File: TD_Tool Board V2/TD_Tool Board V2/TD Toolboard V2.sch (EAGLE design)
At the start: 142 parts, among them J3 430450400CON_430450400_MOL, M1 NMOSFET_WSD3066DN33, M2 CJ3400, M3 CJ3400, M4 CJ3400, P1 TPS54202_BUCKCONV, P2 3.3V, U1 RP2040IC57_RP2040-L, U2 W25Q128JVSIQSOIC_128JVSIQ_WIN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, U3 SN65HVD1050DRD8-L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

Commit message: TMC routed
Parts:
- removed IO3: TEST-POINT3, SparkFun-Connectors:TEST-POINT3
- removed X4: JST-XH-04-PIN-LONG-PAD, Rembrandt Electronics - JST XH Connectors v1-0:JST-XH-04-PIN-LONG-PAD
- added EXTRUDER: JST-XH-04-PIN-LONG-PAD, Rembrandt Electronics - JST XH Connectors v1-0:JST-XH-04-PIN-LONG-PAD
- L2: value ACM2012-201-2P-T002ACM2012_TDK -> ACM2012
- U3: value SN65HVD1050DRD8-L -> SN65HVD
- U7: value TMC2209-LA-TQFN28_5X5_3X8_EPAD_TRI -> TMC2209
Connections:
- net +5V: no longer IO3.1
- net A1: now also EXTRUDER-2.S; no longer X4-2.S
- net A2: now also EXTRUDER-1.S; no longer X4-1.S
- net B1: now also EXTRUDER-3.S; no longer X4-3.S
- net B2: now also EXTRUDER-4.S; no longer X4-4.S
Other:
- moved on the sheet: A1, A2, B1, B2
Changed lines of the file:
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@@
 <part name="SUPPLY48" library="Power_Symbols" deviceset="+3.3V" device="" value="+3.3V"/>
 <part name="SUPPLY49" library="Power_Symbols" deviceset="+3.3V" device="" value="+3.3V"/>
-<part name="U3" library="Fracktal Misc Lib" library_urn="urn:adsk.wipprod:fs.file:vf.Pfq9Q3azRLuASzDebw0K2A" deviceset="SN65HVD1050DR" device="D8-L">
+<part name="U3" library="Fracktal Misc Lib" library_urn="urn:adsk.wipprod:fs.file:vf.Pfq9Q3azRLuASzDebw0K2A" deviceset="SN65HVD1050DR" device="D8-L" value="SN65HVD">
 <attribute name="LCSCPN#" value="C14019"/>
 </part>
@@
 <attribute name="LCSCPN#" value="C25079"/>
 </part>
-<part name="L2" library="2023-04-02_14-21-16_Library" deviceset="ACM2012-201-2P-T002" device="ACM2012_TDK">
+<part name="L2" library="2023-04-02_14-21-16_Library" deviceset="ACM2012-201-2P-T002" device="ACM2012_TDK" value="ACM2012">
 <attribute name="LCSCPN#" value="C3029258"/>
 </part>
 <part name="SJ1" library="SparkFun-Retired" deviceset="SOLDERJUMPER" device="TRACE"/>
-<part name="U7" library="Fracktal Misc Lib" library_urn="urn:adsk.wipprod:fs.file:vf.Pfq9Q3azRLuASzDebw0K2A" deviceset="TMC2209-LA-T" device="QFN28_5X5_3X8_EPAD_TRI" value="TMC2209-LA-TQFN28_5X5_3X8_EPAD_TRI">
+<part name="U7" library="Fracktal Misc Lib" library_urn="urn:adsk.wipprod:fs.file:vf.Pfq9Q3azRLuASzDebw0K2A" deviceset="TMC2209-LA-T" device="QFN28_5X5_3X8_EPAD_TRI" value="TMC2209">
 <attribute name="LCSCPN#" value="C2150710"/>
 </part>
@@
 <part name="IO1" library="SparkFun-Connectors" library_urn="urn:adsk.eagle:library:513" deviceset="TEST-POINT" device="3" package3d_urn="urn:adsk.eagle:package:38286/1"/>
 <part name="IO2" library="SparkFun-Connectors" library_urn="urn:adsk.eagle:library:513" deviceset="TEST-POINT" device="3" package3d_urn="urn:adsk.eagle:package:38286/1"/>
-<part name="IO3" library="SparkFun-Connectors" library_urn="urn:adsk.eagle:library:513" deviceset="TEST-POINT" device="3" package3d_urn="urn:adsk.eagle:package:38286/1"/>
 <part name="SJ3" library="SparkFun-Retired" deviceset="SOLDERJUMPER" device="TRACE"/>
 <part name="SUPPLY68" library="Power_Symbols" deviceset="+12V" device="" value="+24V"/>
@@
 <part name="B1" library="SparkFun-Connectors" library_urn="urn:adsk.eagle:library:513" deviceset="TEST-POINT" device="3X4" package3d_urn="urn:adsk.eagle:package:38287/1"/>
 <part name="B2" library="SparkFun-Connectors" library_urn="urn:adsk.eagle:library:513" deviceset="TEST-POINT" device="3X4" package3d_urn="urn:adsk.eagle:package:38287/1"/>
-<part name="X4" library="Rembrandt Electronics - JST XH Connectors v1-0" deviceset="JST-XH-04-PIN" device="-LONG-PAD">
+<part name="EXTRUDER" library="Rembrandt Electronics - JST XH Connectors v1-0" deviceset="JST-XH-04-PIN" device="-LONG-PAD">
 <attribute name="EXTRUDER" value=""/>
 </part>
@@
 <attribute name="NAME" x="356.87" y="-131.064" size="1.27" layer="95" font="vector" rot="R180" align="center-left"/>
 </instance>
-<instance part="IO3" gate="G$1" x="370.84" y="-120.904" smashed="yes" rot="R180">
-<attribute name="NAME" x="367.03" y="-120.904" size="1.27" layer="95" font="vector" rot="R180" align="center-left"/>
-</instance>
 <instance part="SJ3" gate="1" x="439.42" y="-104.14" smashed="yes">
 <attribute name="NAME" x="436.88" y="-101.6" size="1.778" layer="95"/>
@@
 <attribute name="NAME" x="429.26" y="-208.28" size="1.778" layer="95" font="vector"/>
 </instance>
-<instance part="A2" gate="G$1" x="368.3" y="-264.16" smashed="yes">
-<attribute name="NAME" x="373.38" y="-264.16" size="1.778" layer="95" font="vector"/>
-</instance>
-<instance part="A1" gate="G$1" x="368.3" y="-261.62" smashed="yes">
-<attribute name="NAME" x="373.38" y="-261.62" size="1.778" layer="95" font="vector"/>
-</instance>
-<instance part="B1" gate="G$1" x="368.3" y="-259.08" smashed="yes">
-<attribute name="NAME" x="373.38" y="-259.08" size="1.778" layer="95" font="vector"/>
-</instance>
-<instance part="B2" gate="G$1" x="368.3" y="-256.54" smashed="yes">
-<attribute name="NAME" x="373.38" y="-256.54" size="1.778" layer="95" font="vector"/>
-</instance>
-<instance part="X4" gate="-1" x="340.36" y="-264.16" smashed="yes" rot="R180">
-<attribute name="NAME" x="337.82" y="-263.398" size="1.524" layer="95" rot="R180"/>
-<attribute name="VALUE" x="341.122" y="-265.557" size="1.778" layer="96" rot="R180"/>
-<attribute name="EXTRUDER" x="342.9" y="-254" size="1.778" layer="96" rot="R180" display="name"/>
-</instance>
-<instance part="X4" gate="-2" x="340.36" y="-261.62" smashed="yes" rot="R180">
-<attribute name="NAME" x="337.82" y="-260.858" size="1.524" layer="95" rot="R180"/>
-</instance>
-<instance part="X4" gate="-3" x="340.36" y="-259.08" smashed="yes" rot="R180">
-<attribute name="NAME" x="337.82" y="-258.318" size="1.524" layer="95" rot="R180"/>
-</instance>
-<instance part="X4" gate="-4" x="340.36" y="-256.54" smashed="yes" rot="R180">
-<attribute name="NAME" x="337.82" y="-255.778" size="1.524" layer="95" rot="R180"/>
+<instance part="A2" gate="G$1" x="393.7" y="-264.16" smashed="yes">
+<attribute name="NAME" x="398.78" y="-264.16" size="1.778" layer="95" font="vector"/>
+</instance>
+<instance part="A1" gate="G$1" x="393.7" y="-261.62" smashed="yes">
+<attribute name="NAME" x="398.78" y="-261.62" size="1.778" layer="95" font="vector"/>
+</instance>
+<instance part="B1" gate="G$1" x="393.7" y="-259.08" smashed="yes">
+<attribute name="NAME" x="398.78" y="-259.08" size="1.778" layer="95" font="vector"/>
+</instance>
+<instance part="B2" gate="G$1" x="393.7" y="-256.54" smashed="yes">
+<attribute name="NAME" x="398.78" y="-256.54" size="1.778" layer="95" font="vector"/>
+</instance>
+<instance part="EXTRUDER" gate="-1" x="365.76" y="-264.16" smashed="yes" rot="R180">
+<attribute name="NAME" x="363.22" y="-263.398" size="1.524" layer="95" rot="R180"/>
+<attribute name="VALUE" x="366.522" y="-265.557" size="1.778" layer="96" rot="R180"/>
+<attribute name="EXTRUDER" x="368.3" y="-254" size="1.778" layer="96" rot="R180" display="name"/>
+</instance>
+<instance part="EXTRUDER" gate="-2" x="365.76" y="-261.62" smashed="yes" rot="R180">
+<attribute name="NAME" x="363.22" y="-260.858" size="1.524" layer="95" rot="R180"/>
+</instance>
+<instance part="EXTRUDER" gate="-3" x="365.76" y="-259.08" smashed="yes" rot="R180">
+<attribute name="NAME" x="363.22" y="-258.318" size="1.524" layer="95" rot="R180"/>
+</instance>
+<instance part="EXTRUDER" gate="-4" x="365.76" y="-256.54" smashed="yes" rot="R180">
+<attribute name="NAME" x="363.22" y="-255.778" size="1.524" layer="95" rot="R180"/>
 </instance>
 <instance part="M2" gate="G$1" x="373.38" y="-370.84" smashed="yes">
@@
 <wire x1="403.86" y1="-127" x2="383.54" y2="-127" width="0.1524" layer="91"/>
 <pinref part="SUPPLY34" gate="G$1" pin="+5V"/>
-<wire x1="383.54" y1="-127" x2="383.54" y2="-119.38" width="0.1524" layer="91"/>
-<junction x="383.54" y="-127"/>
-<pinref part="IO3" gate="G$1" pin="1"/>
-<wire x1="383.54" y1="-119.38" x2="370.84" y2="-119.38" width="0.1524" layer="91"/>
-<wire x1="370.84" y1="-119.38" x2="370.84" y2="-120.904" width="0.1524" layer="91"/>
 </segment>
 </net>
@@
 </segment>
 <segment>
-<label x="358.14" y="-256.54" size="1.27" layer="95" xref="yes"/>
+<label x="383.54" y="-256.54" size="1.27" layer="95" xref="yes"/>
 <pinref part="B2" gate="G$1" pin="1"/>
-<wire x1="368.3" y1="-256.54" x2="342.9" y2="-256.54" width="0.1524" layer="91"/>
-<pinref part="X4" gate="-4" pin="S"/>
+<wire x1="393.7" y1="-256.54" x2="368.3" y2="-256.54" width="0.1524" layer="91"/>
+<pinref part="EXTRUDER" gate="-4" pin="S"/>
 </segment>
 </net>
@@
 </segment>
 <segment>
-<wire x1="342.9" y1="-264.16" x2="368.3" y2="-264.16" width="0.1524" layer="91"/>
-<label x="358.14" y="-264.16" size="1.27" layer="95" xref="yes"/>
+<wire x1="368.3" y1="-264.16" x2="393.7" y2="-264.16" width="0.1524" layer="91"/>
+<label x="383.54" y="-264.16" size="1.27" layer="95" xref="yes"/>
 <pinref part="A2" gate="G$1" pin="1"/>
-<pinref part="X4" gate="-1" pin="S"/>
+<pinref part="EXTRUDER" gate="-1" pin="S"/>
 </segment>
 </net>
@@
 </segment>
 <segment>
-<wire x1="342.9" y1="-261.62" x2="368.3" y2="-261.62" width="0.1524" layer="91"/>
-<label x="358.14" y="-261.62" size="1.27" layer="95" xref="yes"/>
+<wire x1="368.3" y1="-261.62" x2="393.7" y2="-261.62" width="0.1524" layer="91"/>
+<label x="383.54" y="-261.62" size="1.27" layer="95" xref="yes"/>
 <pinref part="A1" gate="G$1" pin="1"/>
-<pinref part="X4" gate="-2" pin="S"/>
+<pinref part="EXTRUDER" gate="-2" pin="S"/>
 </segment>
 </net>
@@
 </segment>
 <segment>
-<wire x1="342.9" y1="-259.08" x2="368.3" y2="-259.08" width="0.1524" layer="91"/>
-<label x="358.14" y="-259.08" size="1.27" layer="95" xref="yes"/>
+<wire x1="368.3" y1="-259.08" x2="393.7" y2="-259.08" width="0.1524" layer="91"/>
+<label x="383.54" y="-259.08" size="1.27" layer="95" xref="yes"/>
 <pinref part="B1" gate="G$1" pin="1"/>
-<pinref part="X4" gate="-3" pin="S"/>
-</segment>
-</net>
+<pinref part="EXTRUDER" gate="-3" pin="S"/>
+</segment>
+</net>

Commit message: Placed other connectors and re arranged adxl345
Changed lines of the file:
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@@
 </segment>
 <segment>
-<wire x1="378.46" y1="-363.29" x2="386.08" y2="-363.29" width="0.1524" layer="91"/>
 <wire x1="386.08" y1="-363.29" x2="386.08" y2="-363.22" width="0.1524" layer="91"/>
 <pinref part="SUPPLY87" gate="G$1" pin="+12V"/>
@@
 <pinref part="C42" gate="G$1" pin="1"/>
 <junction x="386.08" y="-363.22"/>
-<wire x1="378.46" y1="-363.29" x2="378.46" y2="-342.9" width="0.1524" layer="91"/>
+<wire x1="386.08" y1="-363.22" x2="378.46" y2="-363.22" width="0.1524" layer="91"/>
 <pinref part="X5" gate="-2" pin="S"/>
+<wire x1="378.46" y1="-363.22" x2="378.46" y2="-342.9" width="0.1524" layer="91"/>
 </segment>
 <segment>
@@
 <segment>
 <pinref part="M2" gate="G$1" pin="D"/>
+<pinref part="X5" gate="-1" pin="S"/>
 <wire x1="375.92" y1="-365.76" x2="375.92" y2="-342.9" width="0.1524" layer="91"/>
-<pinref part="X5" gate="-1" pin="S"/>
-</segment>
-</net>
+</segment>
+</net>

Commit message: Finished routing all components
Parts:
- removed FD1, FD2, FD3: FIDUCIAL, CDC Library:FIDUCIAL
- D9: device LED:CHIP-FLAT-G_0603-0.35MM -> led:LED3MM
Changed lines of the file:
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@@
 <layers>
 <layer number="1" name="Top" color="4" fill="1" visible="no" active="no"/>
+<layer number="2" name="Route2" color="1" fill="3" visible="no" active="no"/>
+<layer number="3" name="Route3" color="4" fill="3" visible="no" active="no"/>
+<layer number="4" name="Route4" color="1" fill="4" visible="no" active="no"/>
+<layer number="5" name="Route5" color="4" fill="4" visible="no" active="no"/>
+<layer number="6" name="Route6" color="1" fill="8" visible="no" active="no"/>
+<layer number="7" name="Route7" color="4" fill="8" visible="no" active="no"/>
+<layer number="8" name="Route8" color="1" fill="2" visible="no" active="no"/>
+<layer number="9" name="Route9" color="4" fill="2" visible="no" active="no"/>
+<layer number="10" name="Route10" color="1" fill="7" visible="no" active="no"/>
+<layer number="11" name="Route11" color="4" fill="7" visible="no" active="no"/>
+<layer number="12" name="Route12" color="1" fill="5" visible="no" active="no"/>
+<layer number="13" name="Route13" color="4" fill="5" visible="no" active="no"/>
+<layer number="14" name="Route14" color="1" fill="6" visible="no" active="no"/>
+<layer number="15" name="Route15" color="4" fill="6" visible="no" active="no"/>
 <layer number="16" name="Bottom" color="1" fill="1" visible="no" active="no"/>
 <layer number="17" name="Pads" color="2" fill="1" visible="no" active="no"/>
@@
 <attribute name="LCSCPN#" value="C25087"/>
 </part>
-<part name="FD1" library="CDC Library" library_urn="urn:adsk.wipprod:fs.file:vf.SXBn864FQp6MR9sO0qnWLQ" deviceset="FIDUCIAL" device="" package3d_urn="urn:adsk.eagle:package:6240632/1"/>
-<part name="FD2" library="CDC Library" library_urn="urn:adsk.wipprod:fs.file:vf.SXBn864FQp6MR9sO0qnWLQ" deviceset="FIDUCIAL" device="" package3d_urn="urn:adsk.eagle:package:6240632/1"/>
-<part name="FD3" library="CDC Library" library_urn="urn:adsk.wipprod:fs.file:vf.SXBn864FQp6MR9sO0qnWLQ" deviceset="FIDUCIAL" device="" package3d_urn="urn:adsk.eagle:package:6240632/1"/>
 <part name="FD4" library="CDC Library" library_urn="urn:adsk.wipprod:fs.file:vf.SXBn864FQp6MR9sO0qnWLQ" deviceset="FIDUCIAL" device="" package3d_urn="urn:adsk.eagle:package:6240632/1"/>
 <part name="FD5" library="CDC Library" library_urn="urn:adsk.wipprod:fs.file:vf.SXBn864FQp6MR9sO0qnWLQ" deviceset="FIDUCIAL" device="" package3d_urn="urn:adsk.eagle:package:6240632/1"/>
@@
 <attribute name="LCSCPN#" value="C25086"/>
 </part>
-<part name="D9" library="LED" deviceset="CHIP-FLAT-G" device="_0603-0.35MM" package3d_urn="urn:adsk.eagle:package:24294786/1" value="LED_G">
+<part name="D9" library="led" library_urn="urn:adsk.eagle:library:259" deviceset="LED" device="3MM" package3d_urn="urn:adsk.eagle:package:15797/1" value="LED_G">
 <attribute name="LCSCPN#" value="C72043"/>
 </part>
@@
 <attribute name="LCSCPN#" x="307.34" y="-17.78" size="1.27" layer="96" rot="R90" align="center-right" display="off"/>
 </instance>
-<instance part="FD1" gate="G$1" x="167.64" y="7.62" smashed="yes"/>
-<instance part="FD2" gate="G$1" x="172.72" y="7.62" smashed="yes"/>
-<instance part="FD3" gate="G$1" x="177.8" y="7.62" smashed="yes"/>
 <instance part="FD4" gate="G$1" x="167.64" y="2.54" smashed="yes"/>
 <instance part="FD5" gate="G$1" x="172.72" y="2.54" smashed="yes"/>
@@
 <instance part="D9" gate="G$1" x="193.04" y="-50.8" smashed="yes" rot="R270">
 <attribute name="NAME" x="187.198" y="-50.546" size="1.778" layer="95" rot="R180" align="top-right"/>
-<attribute name="VALUE" x="186.436" y="-54.356" size="1.778" layer="96" rot="R180" align="top-right"/>
 <attribute name="LCSCPN#" x="193.04" y="-50.8" size="1.778" layer="96" rot="R270" display="off"/>
 </instance>

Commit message: Fixed font sizes, added lables
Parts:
- C_FAN2: value JST-XH-02-PIN-LONG-PAD -> JST-XH
- J3: value 430450400CON_430450400_MOL -> JST-MICROFIT
- U1: value RP2040IC57_RP2040-L -> RP2040
- U2: value W25Q128JVSIQSOIC_128JVSIQ_WIN-L -> W25Q128
- U5: value ADXL345BCCZ-RL -> ADXL345
- U6: value SN74LVC1G17DBVRDBV5-L -> SN74L
- renumbered X2 to CANBUS, X3 to ENDSTOP, X5 to H_FAN, X6 to M_FAN, X7 to C_FAN, X8 to C_FAN2

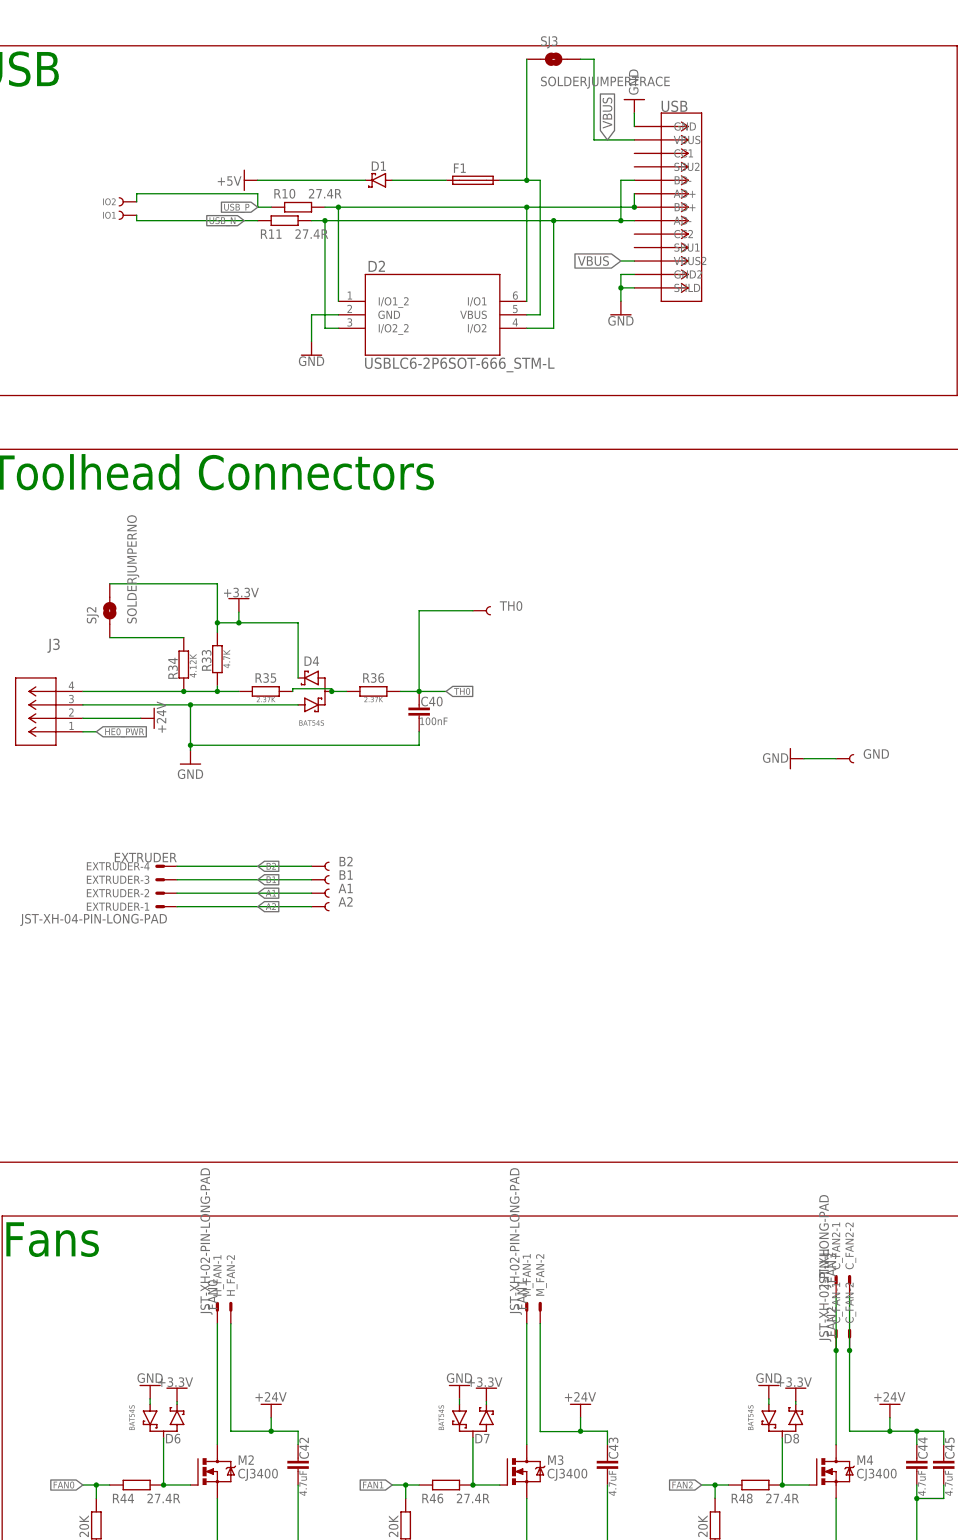
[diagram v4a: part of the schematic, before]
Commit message: minor changes in connector logic
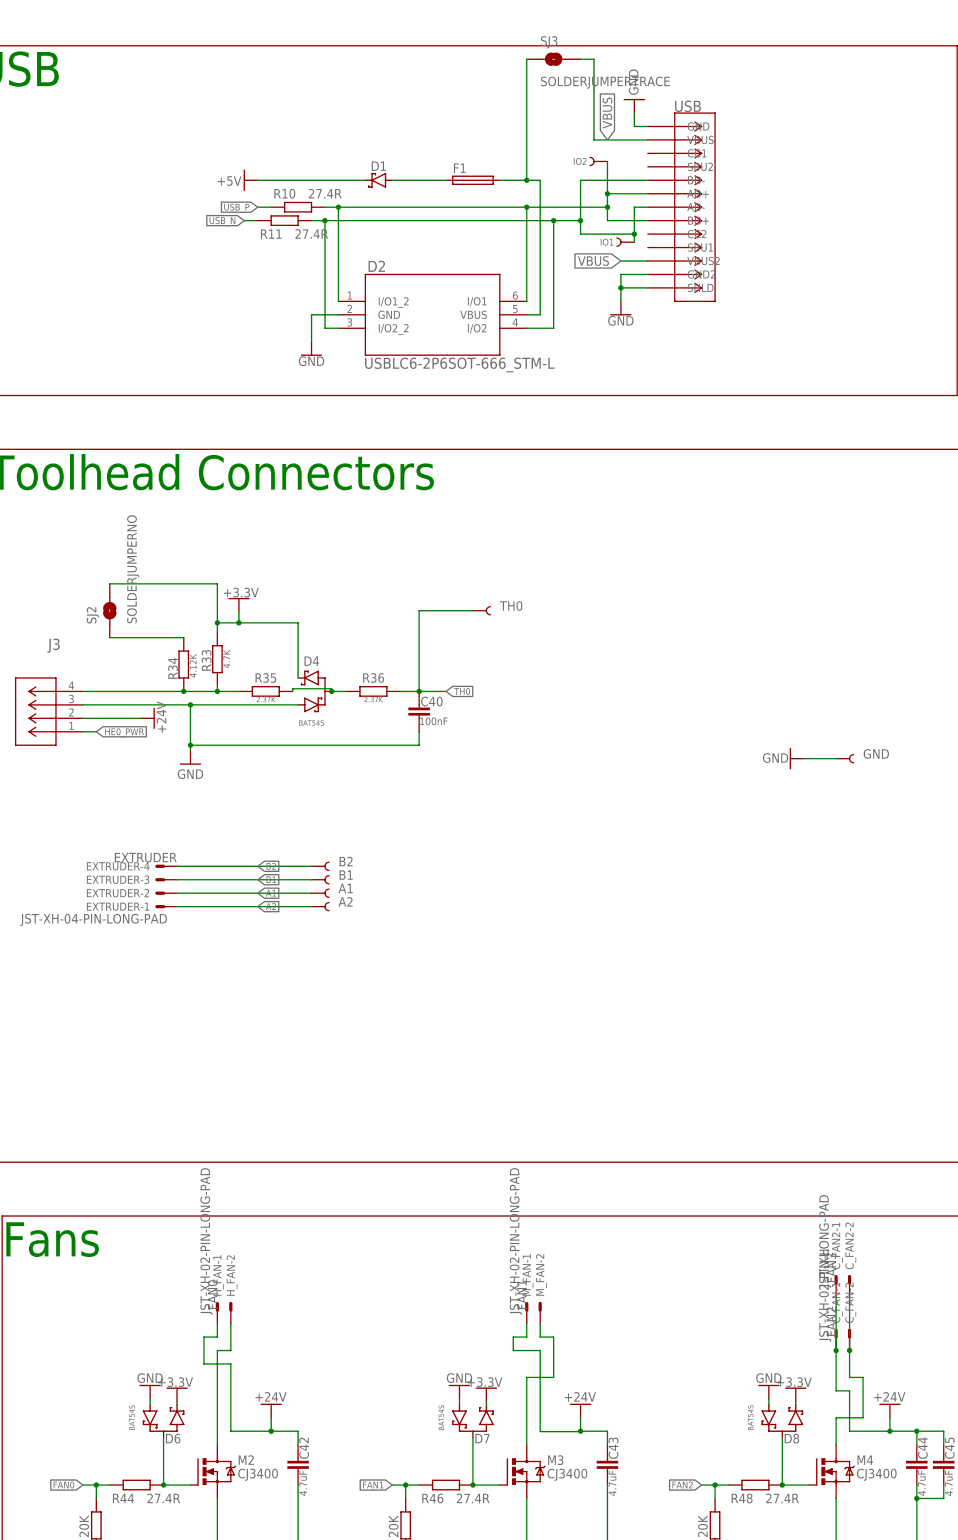
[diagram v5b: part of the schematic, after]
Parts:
- USB: value USB-C(DX07S016JA1R1500) -> USB-C(KH-TYPE-C-16P); device CDC Library:USB-C(DX07S016JA1R1500) -> Fracktal Misc Lib:USB-C(KH-TYPE-C-16P); DATASHEET (none) -> https://datasheet.lcsc.com/lcsc/2009111434_Shenzhen-Kinghel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; VENDOR (none) -> LCSC
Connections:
- removed net FAN1D: M3.D, M_FAN-1.S
- new net N$3: M3.D, M_FAN-2.S
- new net N$4: C_FAN-2.S, C_FAN2-2.S, M4.D
- net +24V: now also C_FAN-1.S, C_FAN2-1.S, H_FAN-1.S; no longer C_FAN-2.S, C_FAN2-2.S, H_FAN-2.S, M_FAN-2.S
- net N$1: now also H_FAN-2.S; no longer H_FAN-1.S
- net N$2: now also M_FAN-1.S; no longer C_FAN-1.S, C_FAN2-1.S, M4.D
- net USB1_N: now also IO1.1
- net USB1_P: now also IO2.1
- net USB_N: no longer IO1.1
- net USB_P: no longer IO2.1
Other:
- moved on the sheet: IO1, IO2, USB
